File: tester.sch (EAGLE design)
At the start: 74 parts, among them IC1 ATmega8/88/168, K1 NA 05W K, M1 SP6000C-180, P1 250, P2 10k lin, Q1 BC847CSMD, Q2 BC847CSMD, Q3 BC807-40SMD, Q4 8,000 MHz, Q5 BC847CSMD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

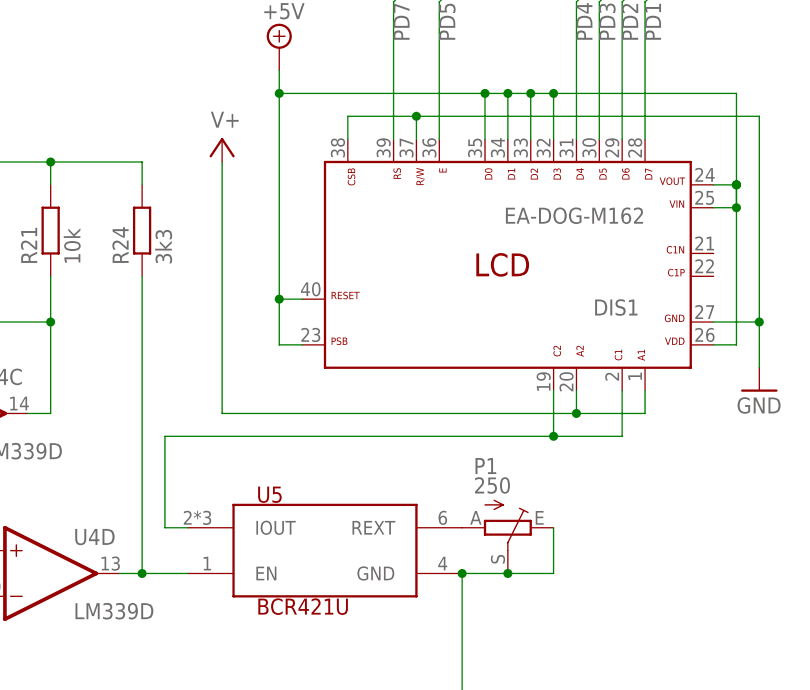
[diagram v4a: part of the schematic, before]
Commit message: power lcd bg led in series
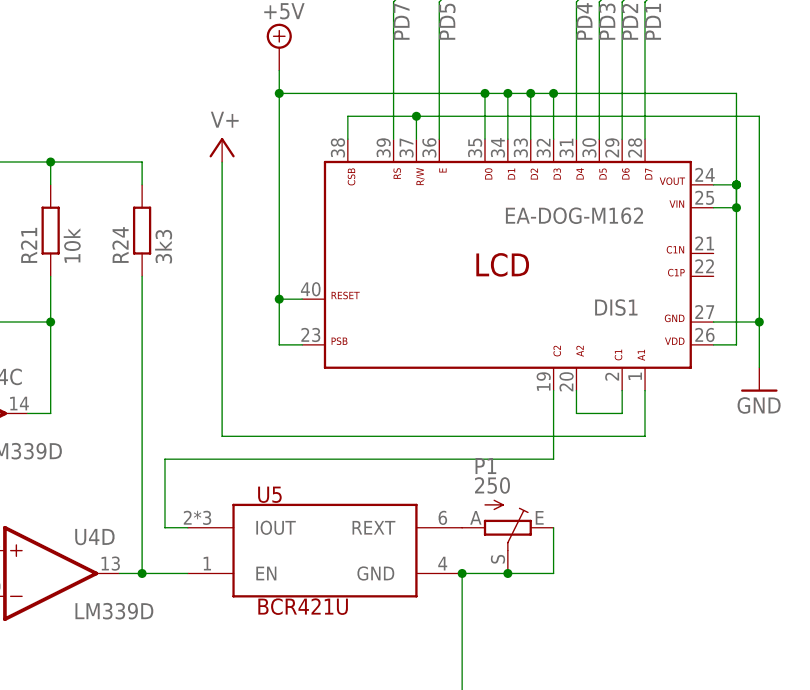
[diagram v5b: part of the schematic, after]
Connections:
- removed net N$18: DIS1.19, DIS1.2, U5.IOUT
- new net N$10: DIS1.19, U5.IOUT
- new net N$2: DIS1.2, DIS1.20
- net V+: no longer DIS1.20
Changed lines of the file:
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@@
 <grid distance="1.27" unitdist="mm" unit="mm" style="lines" multiple="1" display="yes" altdistance="635" altunitdist="mic" altunit="mic"/>
 <layers>
-<layer number="1" name="Top" color="4" fill="1" visible="yes" active="no"/>
-<layer number="2" name="Route2" color="1" fill="3" visible="yes" active="no"/>
-<layer number="3" name="Route3" color="4" fill="3" visible="yes" active="no"/>
-<layer number="4" name="Route4" color="1" fill="4" visible="yes" active="no"/>
-<layer number="5" name="Route5" color="4" fill="4" visible="yes" active="no"/>
-<layer number="6" name="Route6" color="1" fill="8" visible="yes" active="no"/>
-<layer number="7" name="Route7" color="4" fill="8" visible="yes" active="no"/>
-<layer number="8" name="Route8" color="1" fill="2" visible="yes" active="no"/>
-<layer number="9" name="Route9" color="4" fill="2" visible="yes" active="no"/>
-<layer number="10" name="Route10" color="1" fill="7" visible="yes" active="no"/>
-<layer number="11" name="Route11" color="4" fill="7" visible="yes" active="no"/>
-<layer number="12" name="Route12" color="1" fill="5" visible="yes" active="no"/>
-<layer number="13" name="Route13" color="4" fill="5" visible="yes" active="no"/>
-<layer number="14" name="Route14" color="1" fill="6" visible="yes" active="no"/>
-<layer number="15" name="Route15" color="4" fill="6" visible="yes" active="no"/>
-<layer number="16" name="Bottom" color="1" fill="1" visible="yes" active="no"/>
-<layer number="17" name="Pads" color="2" fill="1" visible="yes" active="no"/>
-<layer number="18" name="Vias" color="2" fill="1" visible="yes" active="no"/>
-<layer number="19" name="Unrouted" color="22" fill="1" visible="yes" active="no"/>
-<layer number="20" name="Dimension" color="15" fill="1" visible="yes" active="no"/>
-<layer number="21" name="tPlace" color="7" fill="1" visible="yes" active="no"/>
-<layer number="22" name="bPlace" color="7" fill="1" visible="yes" active="no"/>
-<layer number="23" name="tOrigins" color="15" fill="1" visible="yes" active="no"/>
-<layer number="24" name="bOrigins" color="15" fill="1" visible="yes" active="no"/>
-<layer number="25" name="tNames" color="7" fill="1" visible="yes" active="no"/>
-<layer number="26" name="bNames" color="7" fill="1" visible="yes" active="no"/>
-<layer number="27" name="tValues" color="7" fill="1" visible="yes" active="no"/>
-<layer number="28" name="bValues" color="7" fill="1" visible="yes" active="no"/>
+<layer number="1" name="Top" color="4" fill="1" visible="no" active="no"/>
+<layer number="2" name="Route2" color="1" fill="3" visible="no" active="no"/>
+<layer number="3" name="Route3" color="4" fill="3" visible="no" active="no"/>
+<layer number="4" name="Route4" color="1" fill="4" visible="no" active="no"/>
+<layer number="5" name="Route5" color="4" fill="4" visible="no" active="no"/>
+<layer number="6" name="Route6" color="1" fill="8" visible="no" active="no"/>
+<layer number="7" name="Route7" color="4" fill="8" visible="no" active="no"/>
+<layer number="8" name="Route8" color="1" fill="2" visible="no" active="no"/>
+<layer number="9" name="Route9" color="4" fill="2" visible="no" active="no"/>
+<layer number="10" name="Route10" color="1" fill="7" visible="no" active="no"/>
+<layer number="11" name="Route11" color="4" fill="7" visible="no" active="no"/>
+<layer number="12" name="Route12" color="1" fill="5" visible="no" active="no"/>
+<layer number="13" name="Route13" color="4" fill="5" visible="no" active="no"/>
+<layer number="14" name="Route14" color="1" fill="6" visible="no" active="no"/>
+<layer number="15" name="Route15" color="4" fill="6" visible="no" active="no"/>
+<layer number="16" name="Bottom" color="1" fill="1" visible="no" active="no"/>
+<layer number="17" name="Pads" color="2" fill="1" visible="no" active="no"/>
+<layer number="18" name="Vias" color="2" fill="1" visible="no" active="no"/>
+<layer number="19" name="Unrouted" color="22" fill="1" visible="no" active="no"/>
+<layer number="20" name="Dimension" color="15" fill="1" visible="no" active="no"/>
+<layer number="21" name="tPlace" color="7" fill="1" visible="no" active="no"/>
+<layer number="22" name="bPlace" color="7" fill="1" visible="no" active="no"/>
+<layer number="23" name="tOrigins" color="15" fill="1" visible="no" active="no"/>
+<layer number="24" name="bOrigins" color="15" fill="1" visible="no" active="no"/>
+<layer number="25" name="tNames" color="7" fill="1" visible="no" active="no"/>
+<layer number="26" name="bNames" color="7" fill="1" visible="no" active="no"/>
+<layer number="27" name="tValues" color="7" fill="1" visible="no" active="no"/>
+<layer number="28" name="bValues" color="7" fill="1" visible="no" active="no"/>
 <layer number="29" name="tStop" color="7" fill="3" visible="no" active="no"/>
 <layer number="30" name="bStop" color="7" fill="6" visible="no" active="no"/>
@@
 <layer number="35" name="tGlue" color="7" fill="4" visible="no" active="no"/>
 <layer number="36" name="bGlue" color="7" fill="5" visible="no" active="no"/>
-<layer number="37" name="tTest" color="7" fill="1" visible="yes" active="no"/>
-<layer number="38" name="bTest" color="7" fill="1" visible="yes" active="no"/>
+<layer number="37" name="tTest" color="7" fill="1" visible="no" active="no"/>
+<layer number="38" name="bTest" color="7" fill="1" visible="no" active="no"/>
 <layer number="39" name="tKeepout" color="4" fill="11" visible="no" active="no"/>
 <layer number="40" name="bKeepout" color="1" fill="11" visible="no" active="no"/>
@@
 <layer number="44" name="Drills" color="7" fill="1" visible="no" active="no"/>
 <layer number="45" name="Holes" color="7" fill="1" visible="no" active="no"/>
-<layer number="46" name="Milling" color="3" fill="1" visible="yes" active="no"/>
-<layer number="47" name="Measures" color="7" fill="1" visible="yes" active="no"/>
-<layer number="48" name="Document" color="7" fill="1" visible="yes" active="no"/>
-<layer number="49" name="Reference" color="7" fill="1" visible="yes" active="no"/>
-<layer number="50" name="dxf" color="7" fill="1" visible="yes" active="no"/>
-<layer number="51" name="tDocu" color="7" fill="1" visible="yes" active="no"/>
-<layer number="52" name="bDocu" color="7" fill="1" visible="yes" active="no"/>
-<layer number="53" name="tPadExt" color="7" fill="1" visible="yes" active="no"/>
-<layer number="54" name="bPadExt" color="1" fill="1" visible="yes" active="no"/>
+<layer number="46" name="Milling" color="3" fill="1" visible="no" active="no"/>
+<layer number="47" name="Measures" color="7" fill="1" visible="no" active="no"/>
+<layer number="48" name="Document" color="7" fill="1" visible="no" active="no"/>
+<layer number="49" name="Reference" color="7" fill="1" visible="no" active="no"/>
+<layer number="50" name="dxf" color="7" fill="1" visible="no" active="no"/>
+<layer number="51" name="tDocu" color="7" fill="1" visible="no" active="no"/>
+<layer number="52" name="bDocu" color="7" fill="1" visible="no" active="no"/>
+<layer number="53" name="tPadExt" color="7" fill="1" visible="no" active="no"/>
+<layer number="54" name="bPadExt" color="1" fill="1" visible="no" active="no"/>
 <layer number="91" name="Nets" color="2" fill="1" visible="yes" active="yes"/>
 <layer number="92" name="Busses" color="1" fill="1" visible="yes" active="yes"/>
@@
 </segment>
 </net>
-<net name="N$18" class="0">
-<segment>
-<wire x1="162.56" y1="78.74" x2="154.94" y2="78.74" width="0.1524" layer="91"/>
-<wire x1="154.94" y1="78.74" x2="111.76" y2="78.74" width="0.1524" layer="91"/>
-<wire x1="111.76" y1="78.74" x2="111.76" y2="68.58" width="0.1524" layer="91"/>
-<pinref part="U5" gate="G$1" pin="IOUT"/>
-<wire x1="111.76" y1="68.58" x2="114.3" y2="68.58" width="0.1524" layer="91"/>
-<wire x1="162.56" y1="78.74" x2="162.56" y2="83.82" width="0.1524" layer="91"/>
-<pinref part="DIS1" gate="G$1" pin="2"/>
-<junction x="154.94" y="78.74"/>
-<pinref part="DIS1" gate="G$1" pin="19"/>
-<wire x1="154.94" y1="78.74" x2="154.94" y2="83.82" width="0.1524" layer="91"/>
-</segment>
-</net>
 <net name="+5V/2" class="0">
 <segment>
@@
 </segment>
 <segment>
-<pinref part="DIS1" gate="G$1" pin="20"/>
-<wire x1="157.48" y1="83.82" x2="157.48" y2="81.28" width="0.1524" layer="91"/>
+<wire x1="165.1" y1="78.74" x2="118.11" y2="78.74" width="0.1524" layer="91"/>
+<wire x1="118.11" y1="78.74" x2="118.11" y2="109.22" width="0.1524" layer="91"/>
+<pinref part="SUPPLY5" gate="1" pin="V+"/>
 <pinref part="DIS1" gate="G$1" pin="1"/>
-<wire x1="165.1" y1="83.82" x2="165.1" y2="81.28" width="0.1524" layer="91"/>
-<wire x1="165.1" y1="81.28" x2="157.48" y2="81.28" width="0.1524" layer="91"/>
-<junction x="157.48" y="81.28"/>
-<wire x1="157.48" y1="81.28" x2="118.11" y2="81.28" width="0.1524" layer="91"/>
-<wire x1="118.11" y1="81.28" x2="118.11" y2="109.22" width="0.1524" layer="91"/>
-<pinref part="SUPPLY5" gate="1" pin="V+"/>
+<wire x1="165.1" y1="83.82" x2="165.1" y2="78.74" width="0.1524" layer="91"/>
 </segment>
 </net>
@@
 </segment>
 </net>
+<net name="N$2" class="0">
+<segment>
+<pinref part="DIS1" gate="G$1" pin="20"/>
+<pinref part="DIS1" gate="G$1" pin="2"/>
+<wire x1="162.56" y1="81.28" x2="162.56" y2="83.82" width="0.1524" layer="91"/>
+<wire x1="162.56" y1="81.28" x2="157.48" y2="81.28" width="0.1524" layer="91"/>
+<wire x1="157.48" y1="81.28" x2="157.48" y2="83.82" width="0.1524" layer="91"/>
+</segment>
+</net>
+<net name="N$10" class="0">
+<segment>
+<pinref part="U5" gate="G$1" pin="IOUT"/>
+<pinref part="DIS1" gate="G$1" pin="19"/>
+<wire x1="154.94" y1="76.2" x2="154.94" y2="83.82" width="0.1524" layer="91"/>
+<wire x1="154.94" y1="76.2" x2="111.76" y2="76.2" width="0.1524" layer="91"/>
+<wire x1="111.76" y1="76.2" x2="111.76" y2="68.58" width="0.1524" layer="91"/>
+<wire x1="111.76" y1="68.58" x2="114.3" y2="68.58" width="0.1524" layer="91"/>
+</segment>
+</net>
